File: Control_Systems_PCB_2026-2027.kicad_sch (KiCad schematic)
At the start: 0 parts

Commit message: Fixed: fixed some text and position formatting
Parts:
- added U1: STM32F446VETx, Package_QFP:LQFP-100_14x14mm_P0.5mm, symbol MCU_ST_STM32F4:STM32F446VETx
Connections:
- new net: U1.10 (VSS), U1.27 (VSS), U1.49 (VSS), U1.74 (VSS), U1.99 (VSS)
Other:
- note added: "Control Systems PCB 2026-2027"
- note added: "STM32F446VETx MCU"
- company: (none) -> MetRocketry Control Systems Avionics Subteam
- title: (none) -> Control Systems PCB

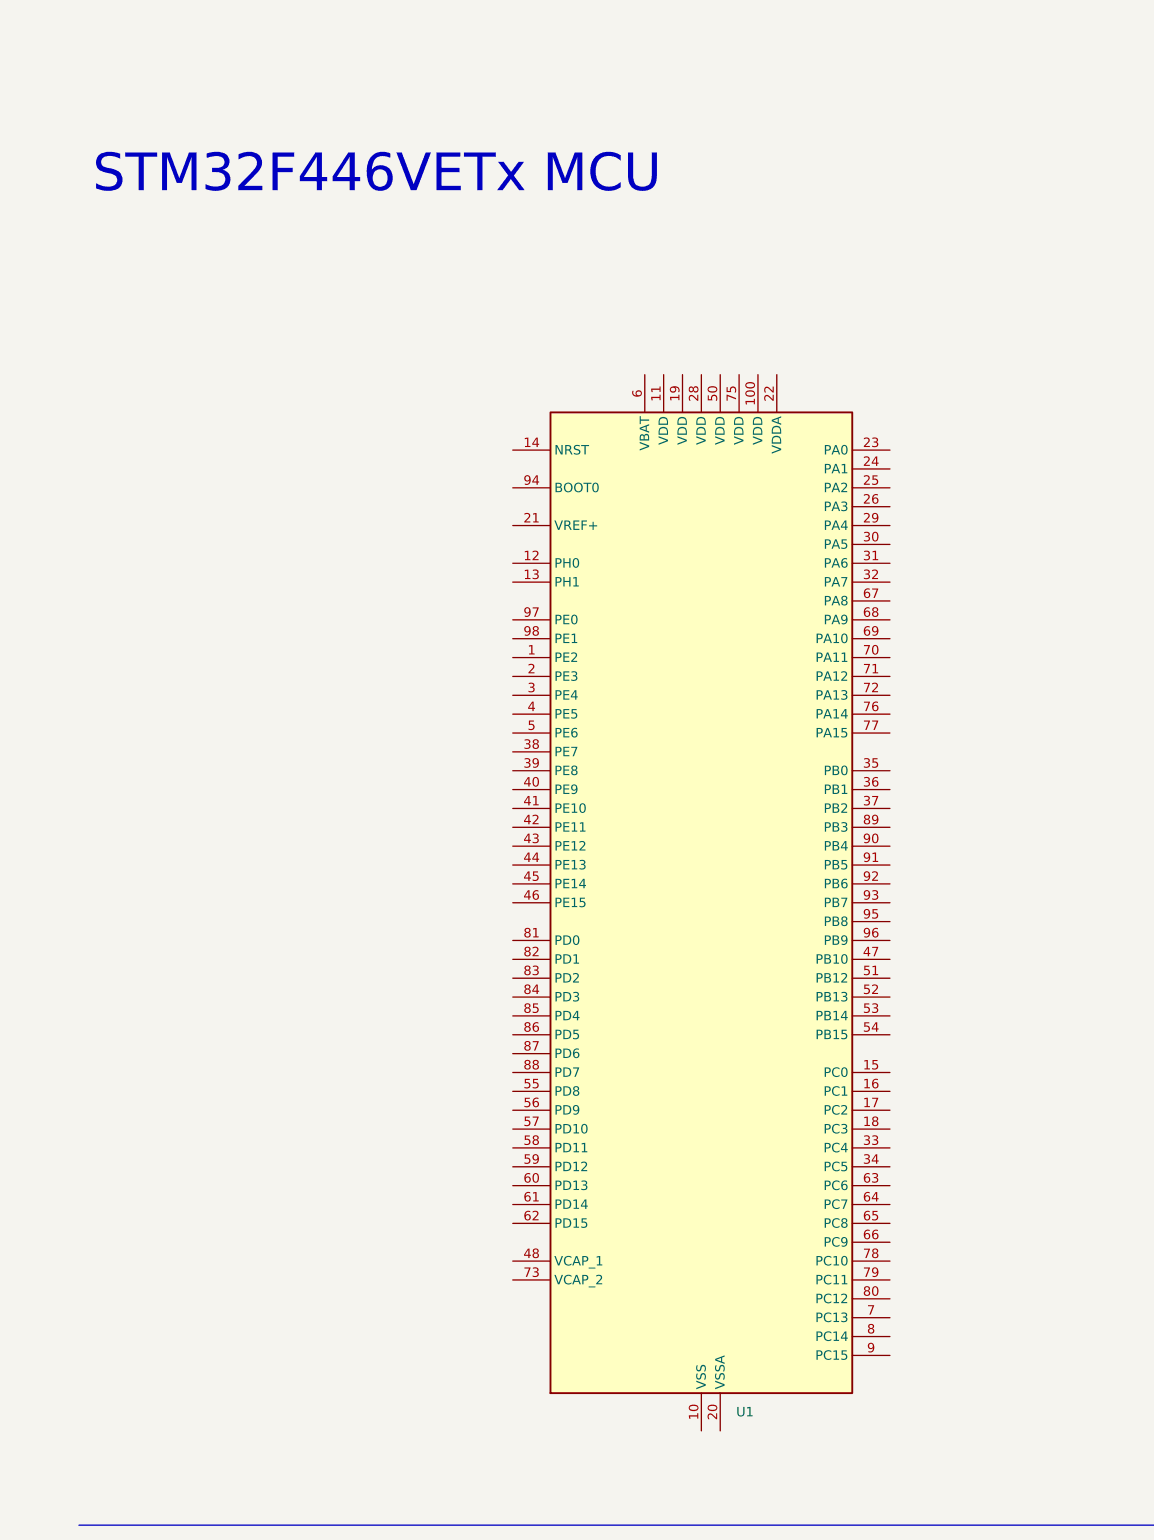
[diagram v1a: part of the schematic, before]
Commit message: Feat: added decoupling capacitors and connected VDDA to VDD
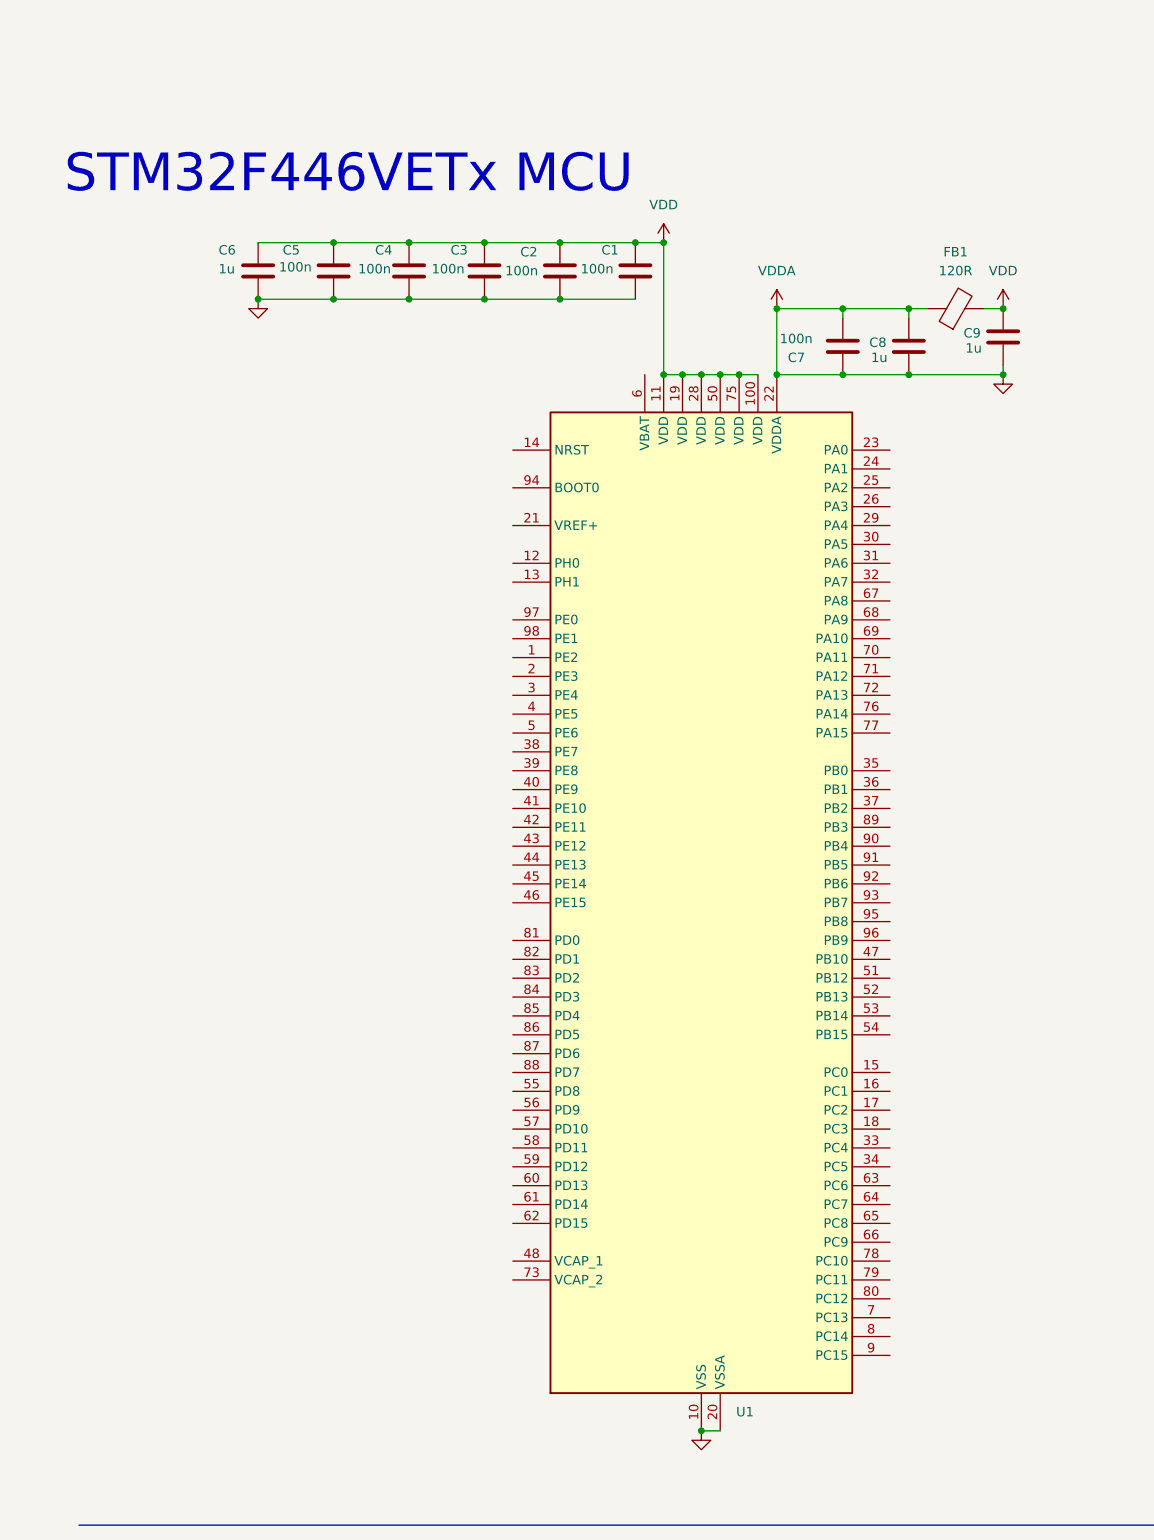
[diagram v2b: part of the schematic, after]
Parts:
- added C1, C2, C3, C4, C5, C7: 100n, symbol Device:C
- added C6, C8, C9: 1u, symbol Device:C
- added FB1: 120R, symbol Device:FerriteBead
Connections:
- net GND: now reaches U1.10 (VSS), U1.27 (VSS), U1.49 (VSS), U1.74 (VSS), U1.99 (VSS)
- net GND: now also U1.20 (VSSA), U1.22 (VDDA), C1.2, C2.2, C3.2, C4.2, C5.2, C6.2, C7.1, C7.2, C8.1, C8.2, C9.2, FB1.1
- net VDD: now reaches U1.100 (VDD)
- net VDD: now also U1.11 (VDD), U1.19 (VDD), U1.28 (VDD), U1.50 (VDD), U1.75 (VDD), C1.1, C2.1, C3.1, C4.1, C5.1, C6.1, C9.1, FB1.2

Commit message: feat: add barometer
* feat: add barometer

* fix(schematic):choose closer pins, however MISO/MOSI and CLK are on opposite sides of the chip regardless

* fix(schematic):choose closer pins, accidentally thought grey = used, and green = unused, fixed mistake

* fix(schematic): fixed the pin outs

* fix(schematic): applied PCB best practices + suggested changes)
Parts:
- added C10: 100n, symbol Device:C
- added U3: MS5611-01BA, Package_LGA:LGA-8_3x5mm_P1.25mm, symbol Sensor_Pressure:MS5611-01BA
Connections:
- net GND: now also C10.2, U3.2 (PS), U3.3 (GND)
- net SPI2_MISO: now reaches U1.53 (PB14)
- net SPI2_MISO: now also U3.6 (SDO)
- net SPI2_MOSI: now reaches U1.54 (PB15)
- net SPI2_MOSI: now also U3.7 (SDI/SDA)
- net PD10_CS: now reaches U1.55 (PD8)
- net PD10_CS: now also U3.4 (CSB), U3.5 (CSB)
- net SPI2_CLK: now reaches U1.64 (PC7)
- net SPI2_CLK: now also U3.8 (SCLK)
- new net +3.3V: C10.1, U3.1 (VDD)

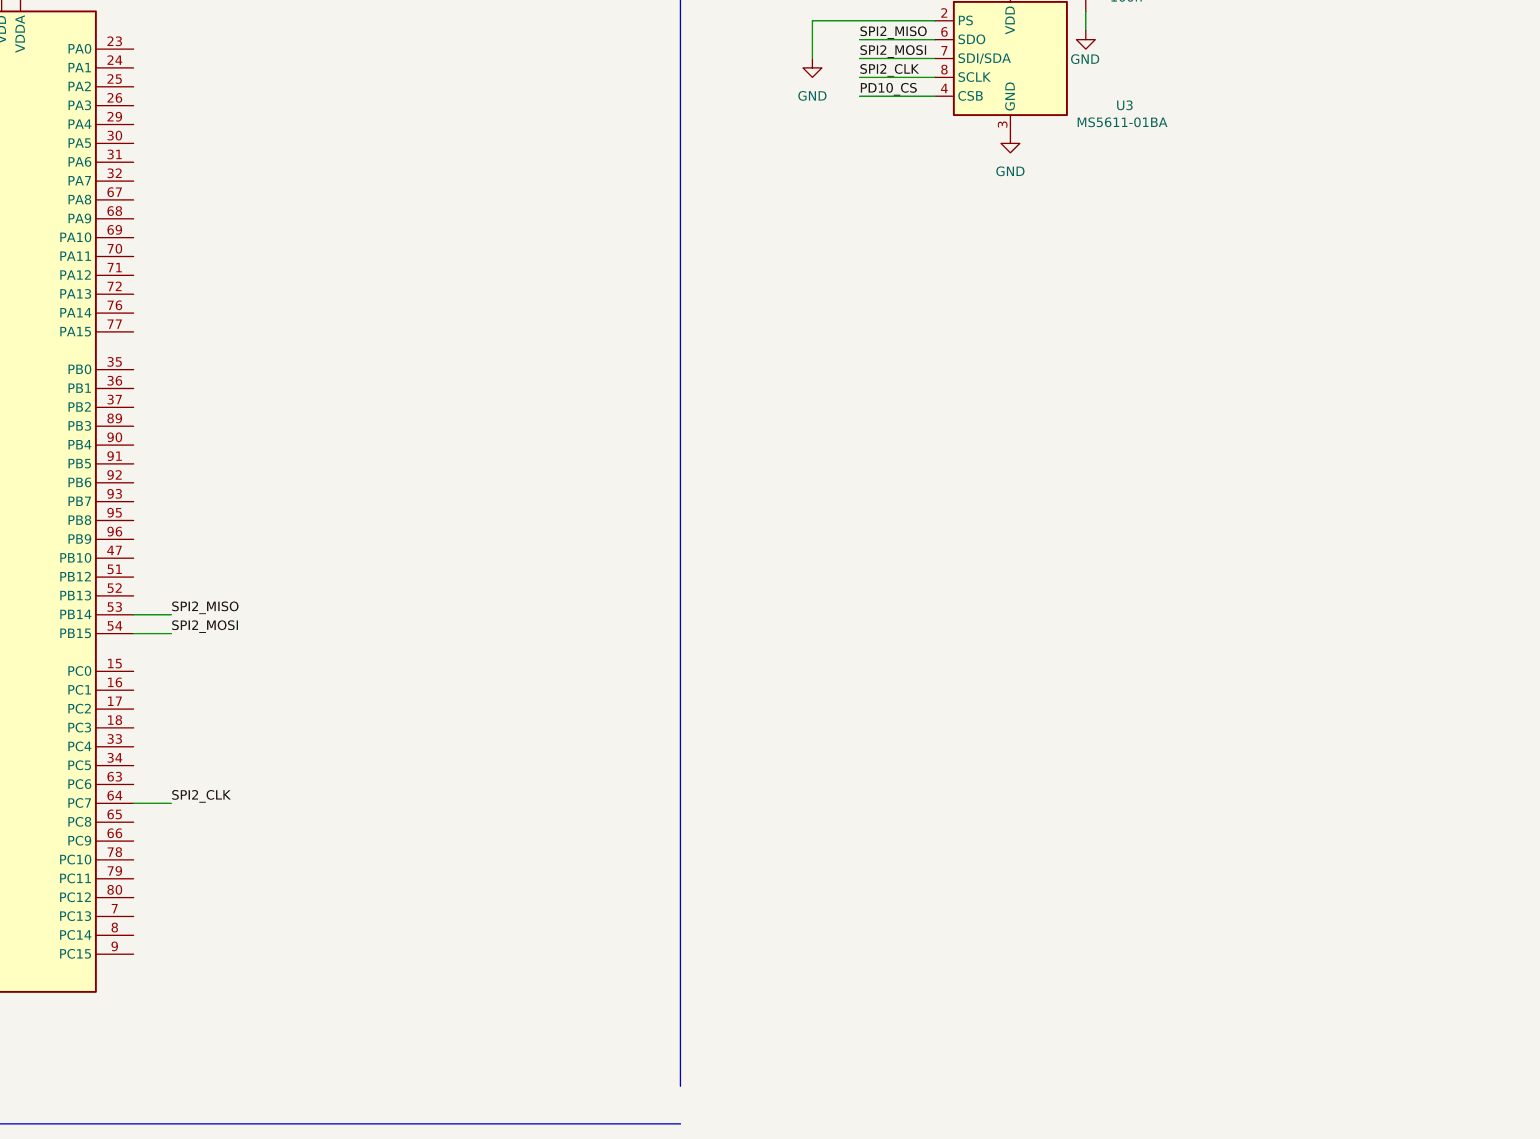
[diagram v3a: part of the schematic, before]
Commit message: Routed magnetometer + installed LED
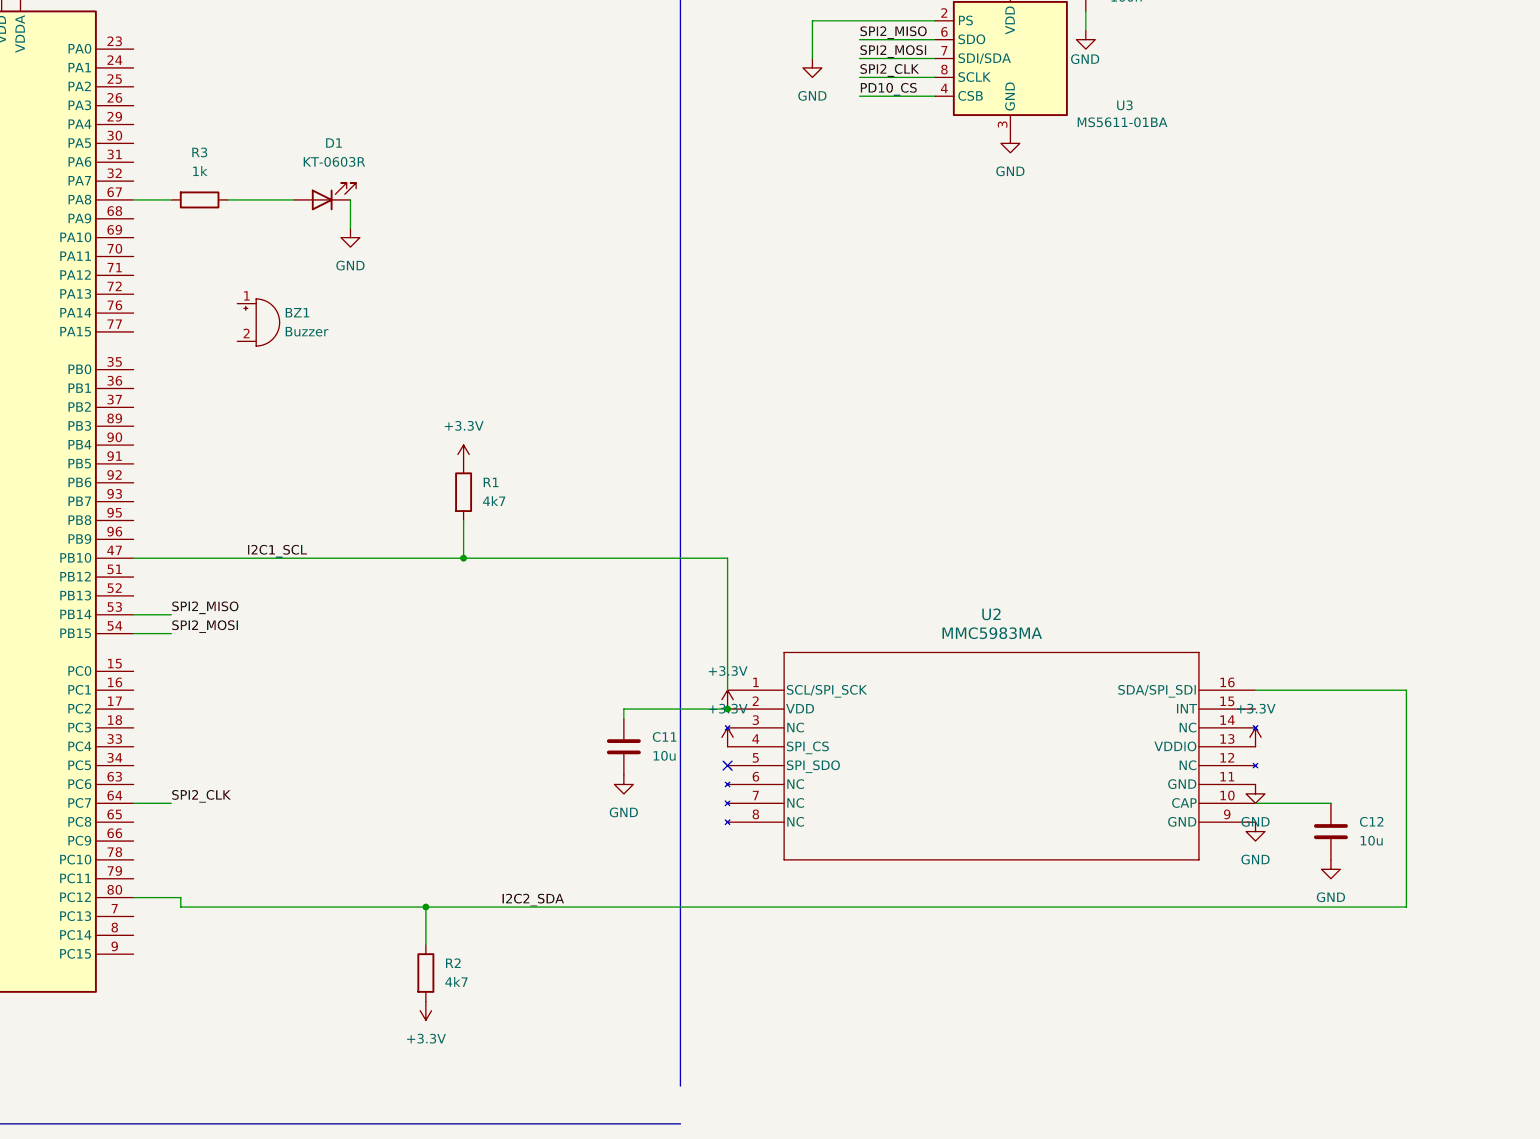
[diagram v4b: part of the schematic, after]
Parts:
- added BZ1: Buzzer, symbol Device:Buzzer
- added C11: 10u, MMC5983MA_MEM, symbol Device:C
- added C12: 10u, symbol Device:C
- added D1: KT-0603R, symbol Device:LED
- added R1: 4k7, Package_DIP:DIP-8_W7.62mm, symbol Device:R
- added R2: 4k7, symbol Device:R
- added R3: 1k, symbol Device:R
- added U2: MMC5983MA, MMC5983MA_MEM, symbol 2026-09-09_19-01-11:MMC5983MA
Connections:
- net +3.3V: now also C11.1, R1.1, R2.2, U2.13 (VDDIO), U2.2 (VDD), U2.4 (SPI_CS)
- net GND: now also C11.2, C12.2, D1.1 (K), U2.11 (GND), U2.9 (GND)
- net I2C1_SCL: now reaches U1.47 (PB10)
- net I2C1_SCL: now also R1.2, U2.1 (SCL/SPI_SCK)
- net at U1.67 (PA8): now also R3.2
- net I2C2_SDA: now reaches U1.80 (PC12)
- net I2C2_SDA: now also R2.1, U2.16 (SDA/SPI_SDI)
- new net: D1.2 (A), R3.1
- new net: C12.1, U2.10 (CAP)
- no-connect marks 0 -> 1
